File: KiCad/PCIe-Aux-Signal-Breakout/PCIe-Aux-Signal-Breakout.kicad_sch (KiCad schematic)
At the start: 8 parts, among them J1 PCIexpress_x1, J2 PCIexpress_bracket, J3 Conn_02x10_Odd_Even, U1 MIC2876-5.0

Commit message: started pcb design
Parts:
- L1: footprint (none) -> PCIe-Aux-Signal-Breakout-Footprint-Library:L_2520_INPAQ
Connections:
- net GND: no longer J3.16 (Pin_16), J3.19 (Pin_19)
- net SMBCLK: now also J3.16 (Pin_16)
- net SMBDAT: now also J3.19 (Pin_19)
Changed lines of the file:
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@@
 	(paper "A4")
-	(junction
-		(at 210.82 85.09)
-		(diameter 0)
-		(color 0 0 0 0)
-	)
 	(junction
 		(at 193.04 74.93)
@@
 	)
 	(junction
-		(at 193.04 90.17)
-		(diameter 0)
-		(color 0 0 0 0)
-	)
-	(junction
 		(at 113.03 162.56)
 		(diameter 0)
@@
 	(wire
 		(pts
+			(xy 208.28 85.09) (xy 217.17 85.09)
+		)
+		(stroke
+			(width 0)
+			(type default)
+		)
+	)
+	(wire
+		(pts
 			(xy 109.22 71.12) (xy 109.22 88.9)
 		)
@@
 	(wire
 		(pts
-			(xy 193.04 74.93) (xy 193.04 90.17)
+			(xy 193.04 74.93) (xy 193.04 92.71)
 		)
 		(stroke
@@
 	(wire
 		(pts
-			(xy 210.82 77.47) (xy 210.82 85.09)
-		)
-		(stroke
-			(width 0)
-			(type default)
-		)
-	)
-	(wire
-		(pts
 			(xy 208.28 82.55) (xy 217.17 82.55)
 		)
@@
 	(wire
 		(pts
-			(xy 210.82 85.09) (xy 210.82 92.71)
+			(xy 210.82 77.47) (xy 210.82 92.71)
 		)
 		(stroke
@@
 	(wire
 		(pts
-			(xy 193.04 90.17) (xy 193.04 92.71)
-		)
-		(stroke
-			(width 0)
-			(type default)
-		)
-	)
-	(wire
-		(pts
 			(xy 49.53 166.37) (xy 57.15 166.37)
 		)
@@
 	(wire
 		(pts
-			(xy 210.82 85.09) (xy 208.28 85.09)
-		)
-		(stroke
-			(width 0)
-			(type default)
-		)
-	)
-	(wire
-		(pts
 			(xy 142.24 93.98) (xy 144.78 93.98)
 		)
@@
 	(wire
 		(pts
-			(xy 195.58 90.17) (xy 193.04 90.17)
-		)
-		(stroke
-			(width 0)
-			(type default)
-		)
-	)
-	(wire
-		(pts
 			(xy 109.22 55.88) (xy 109.22 53.34)
 		)
@@
 		(pts
 			(xy 109.22 63.5) (xy 109.22 71.12)
+		)
+		(stroke
+			(width 0)
+			(type default)
+		)
+	)
+	(wire
+		(pts
+			(xy 187.96 90.17) (xy 195.58 90.17)
 		)
 		(stroke
@@
 		)
 	)
+	(global_label "SMBDAT"
+		(shape input)
+		(at 187.96 90.17 180)
+		(fields_autoplaced yes)
+		(effects
+			(font
+				(size 1.27 1.27)
+			)
+			(justify right)
+		)
+		(property "Intersheetrefs" "${INTERSHEET_REFS}"
+			(at 177.7177 90.17 0)
+			(effects
+				(font
+					(size 1.27 1.27)
+				)
+				(justify right)
+				(hide yes)
+			)
+		)
+	)
 	(global_label "WAKE#"
 		(shape input)
@@
 		(property "Intersheetrefs" "${INTERSHEET_REFS}"
 			(at 153.8733 71.12 0)
+			(effects
+				(font
+					(size 1.27 1.27)
+				)
+				(justify left)
+				(hide yes)
+			)
+		)
+	)
+	(global_label "SMBCLK"
+		(shape input)
+		(at 217.17 85.09 0)
+		(fields_autoplaced yes)
+		(effects
+			(font
+				(size 1.27 1.27)
+			)
+			(justify left)
+		)
+		(property "Intersheetrefs" "${INTERSHEET_REFS}"
+			(at 227.6542 85.09 0)
 			(effects
 				(font
@@
 			)
 		)
-		(property "Footprint" ""
+		(property "Footprint" "PCIe-Aux-Signal-Breakout-Footprint-Library:L_2520_INPAQ"
 			(at 68.58 162.56 0)
 			(effects

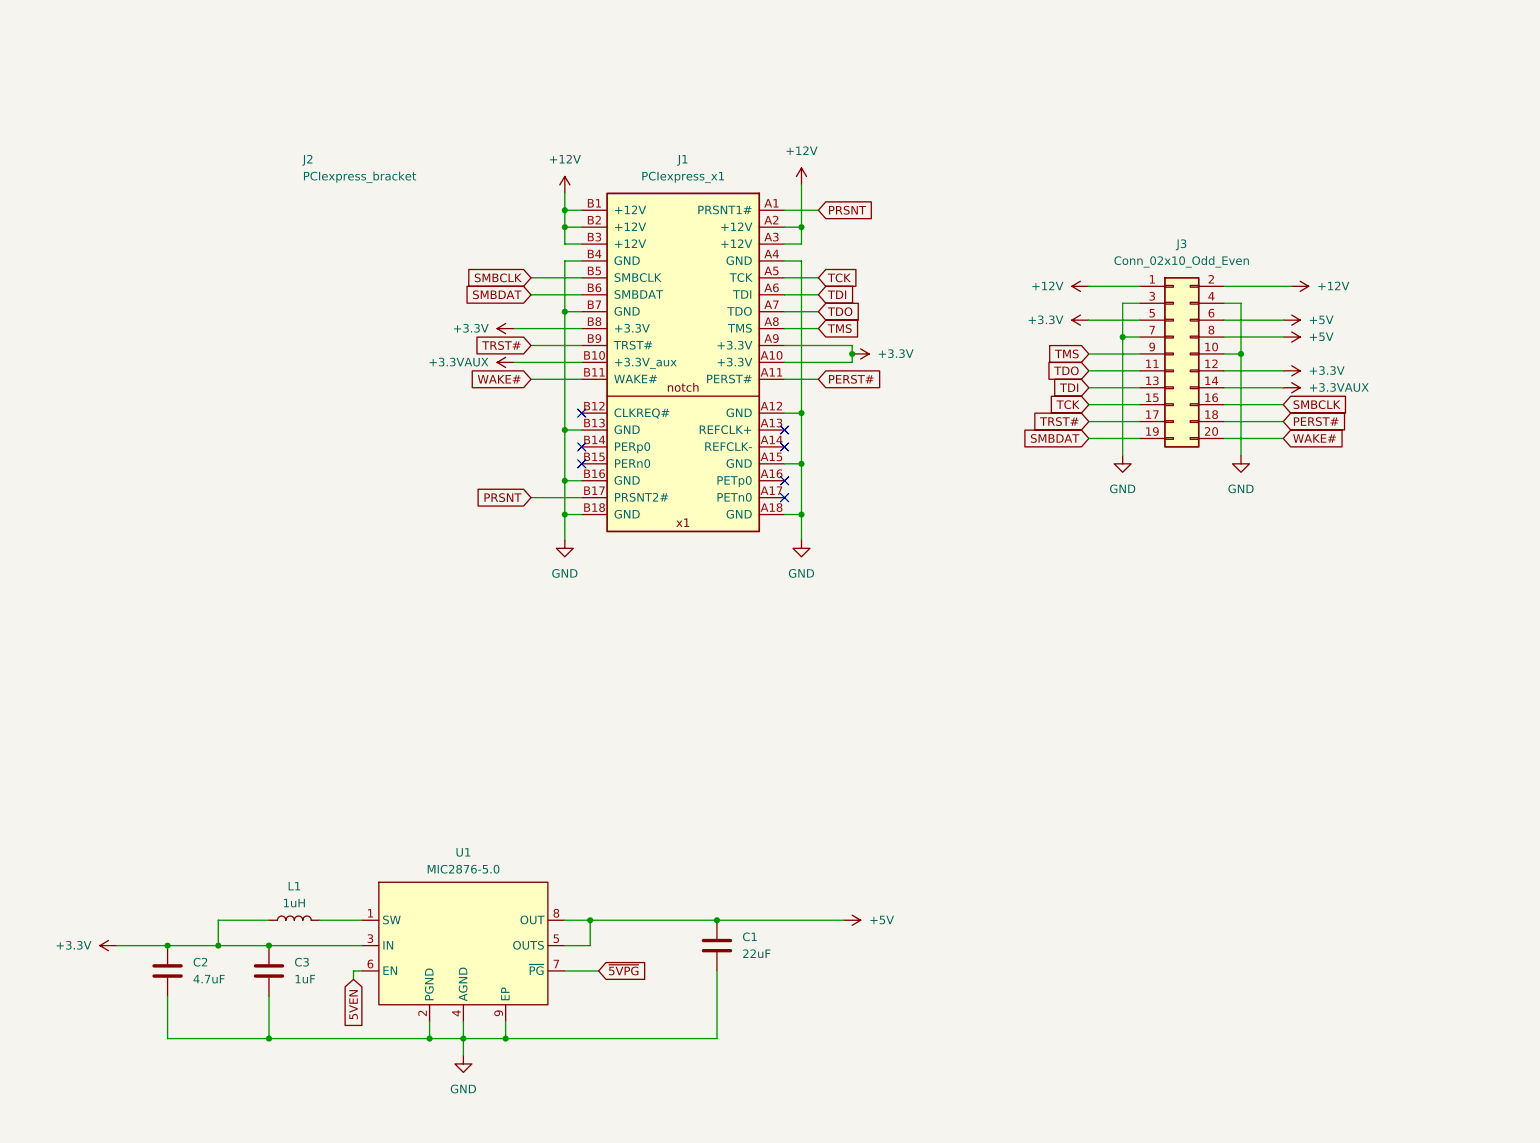
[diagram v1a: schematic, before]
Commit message: finished v1.0 design
finished v1.0 pcb

added low and standard profile pcie bracket with custom connector cutout

made gerber files

added instruction files

added images of the board

added BOM
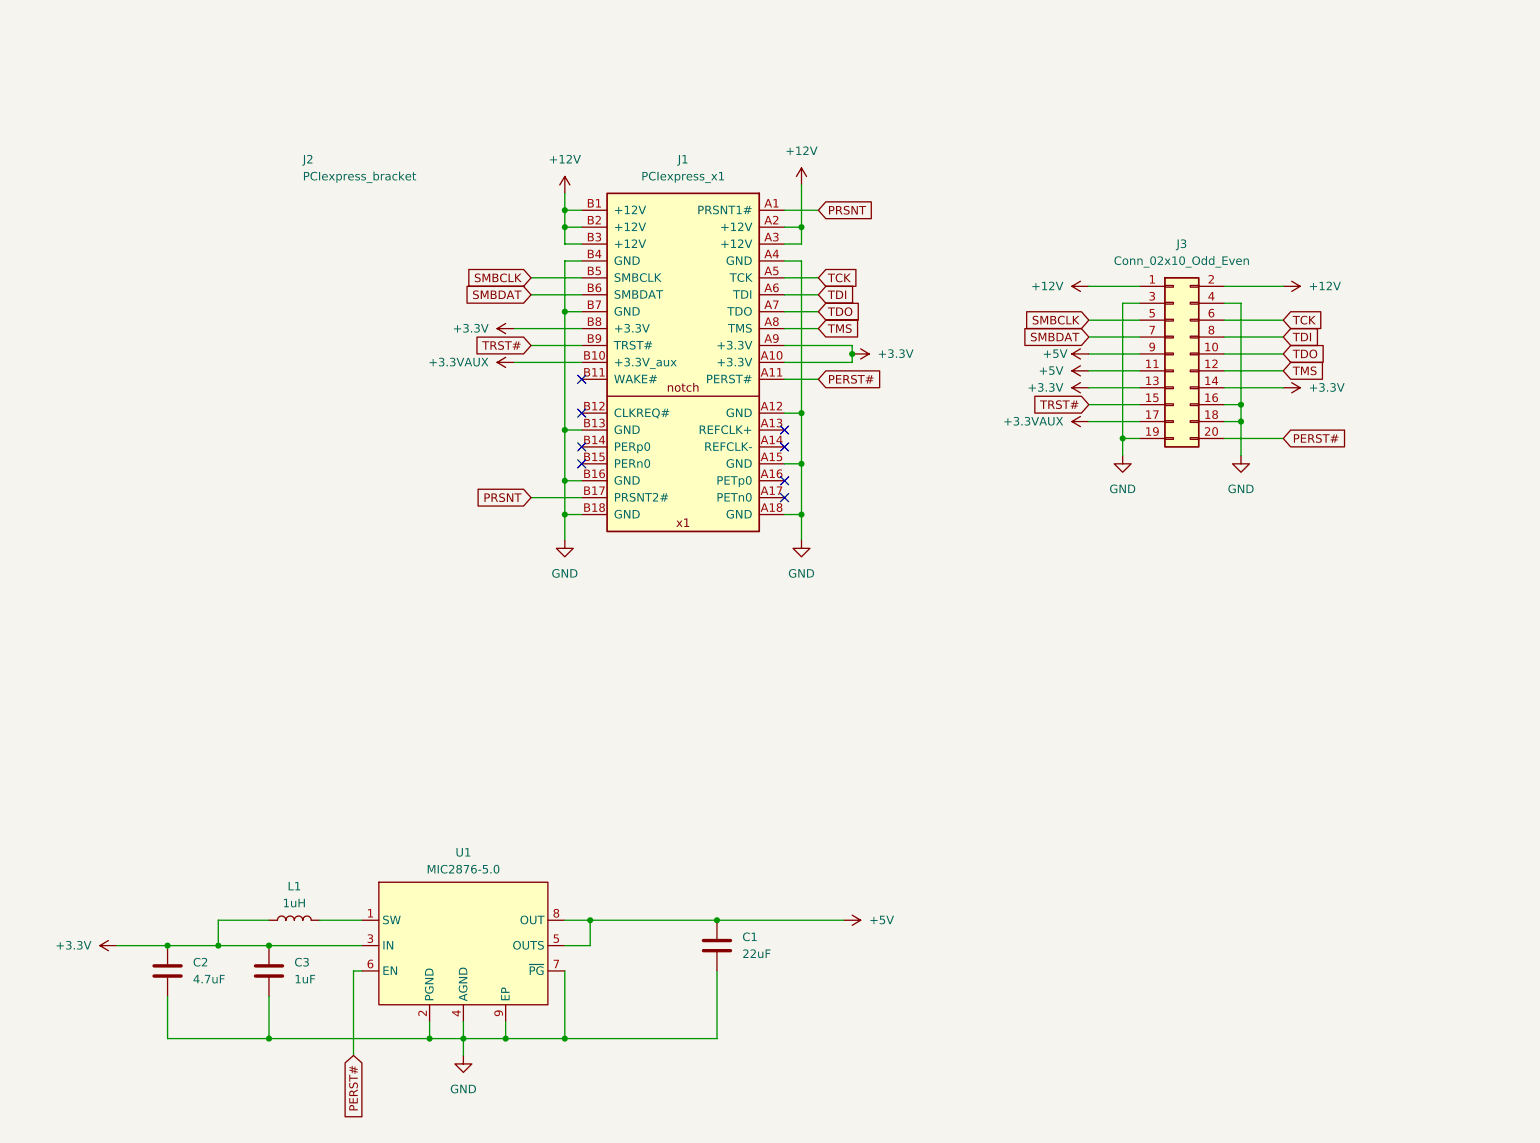
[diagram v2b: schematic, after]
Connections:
- net 5VEN is gone; now on net PERST#: U1.6 (EN)
- net ~{5VPG} is gone; now on net GND: U1.7 (~{PG})
- net +3.3V: now also J3.13 (Pin_13), J3.14 (Pin_14); no longer J3.12 (Pin_12), J3.5 (Pin_5)
- net +3.3VAUX: now also J3.17 (Pin_17); no longer J3.14 (Pin_14)
- net +5V: now also J3.11 (Pin_11), J3.9 (Pin_9); no longer J3.6 (Pin_6), J3.8 (Pin_8)
- net GND: now also J3.16 (Pin_16), J3.18 (Pin_18), J3.19 (Pin_19); no longer J3.10 (Pin_10), J3.7 (Pin_7)
- net PERST#: now also J3.20 (Pin_20); no longer J3.18 (Pin_18)
- net SMBCLK: now also J3.5 (Pin_5); no longer J3.16 (Pin_16)
- net SMBDAT: now also J3.7 (Pin_7); no longer J3.19 (Pin_19)
- net TCK: now also J3.6 (Pin_6); no longer J3.15 (Pin_15)
- net TDI: now also J3.8 (Pin_8); no longer J3.13 (Pin_13)
- net TDO: now also J3.10 (Pin_10); no longer J3.11 (Pin_11)
- net TMS: now also J3.12 (Pin_12); no longer J3.9 (Pin_9)
- net TRST#: now also J3.15 (Pin_15); no longer J3.17 (Pin_17)
- net WAKE#: no longer names the net of J1.B11 (WAKE#)
- net WAKE#: no longer J3.20 (Pin_20)
- no-connect marks 7 -> 8

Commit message: Added Schematic and 3D printing files
-updated board silkscreen

-added STL files for pcie brackets

-added 3d model folder for assembled boards
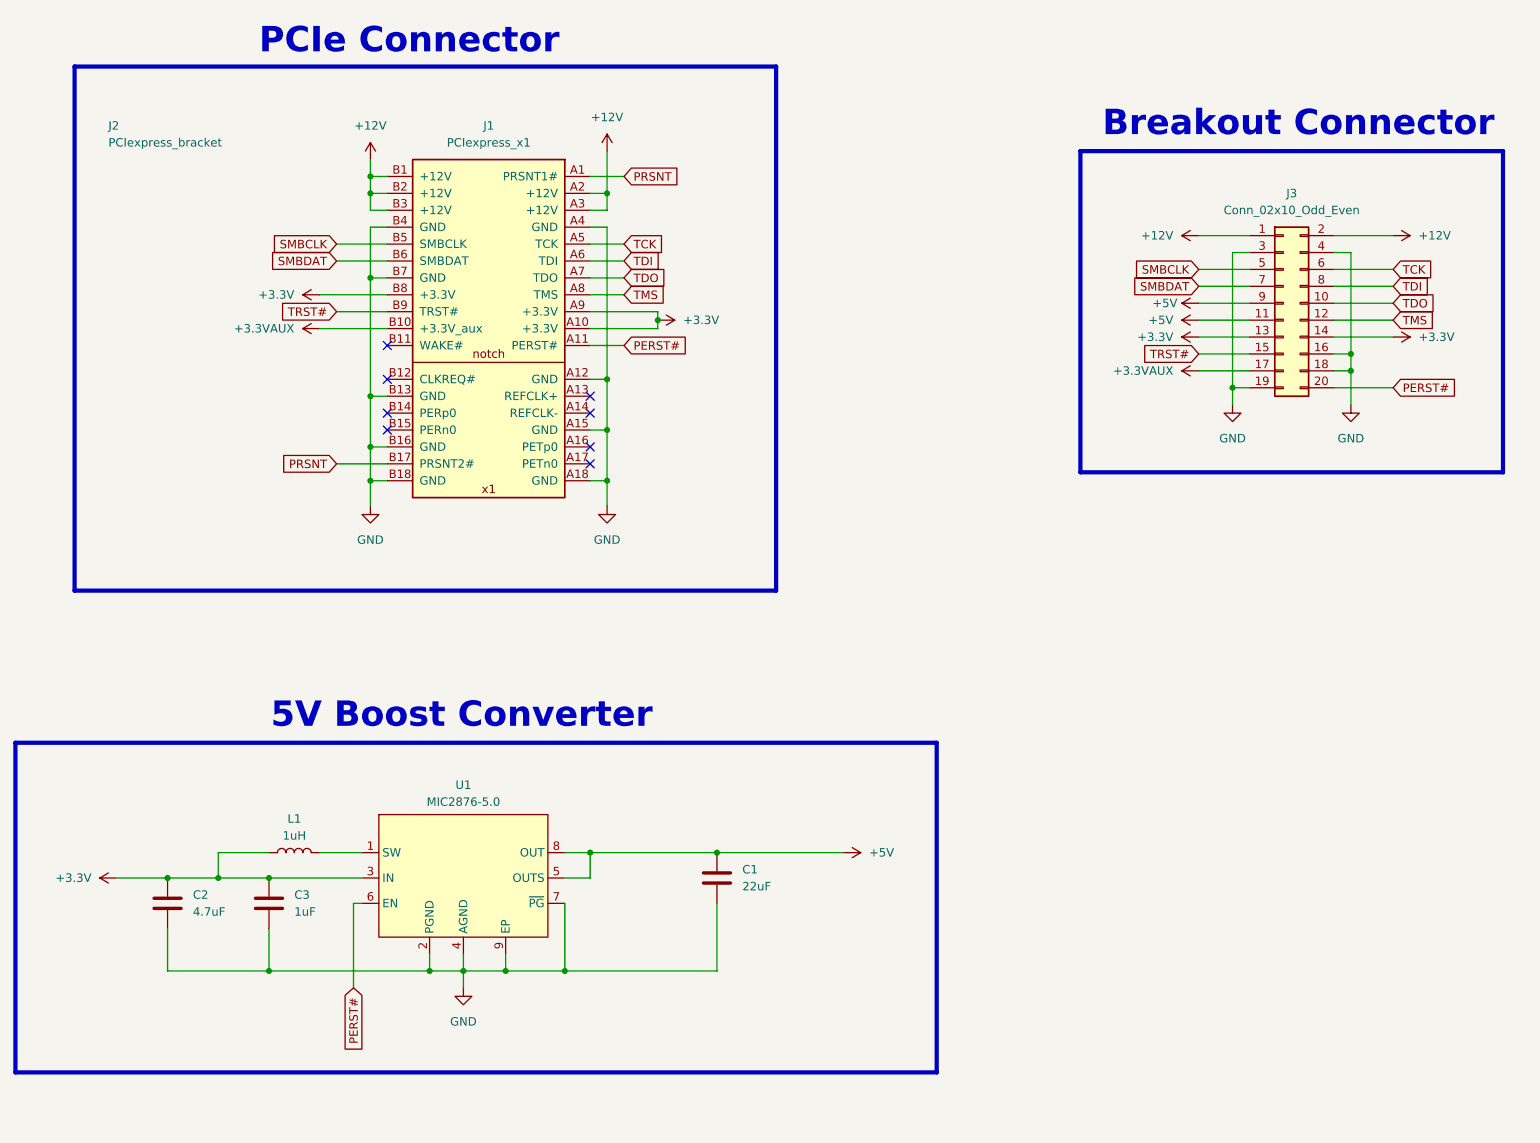
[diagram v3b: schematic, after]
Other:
- note added: "5V Boost Converter"
- note added: "Breakout Connector"
- note added: "PCIe Connector"
- moved on the sheet: C1, C2, C3, J1, J3, L1, U1
